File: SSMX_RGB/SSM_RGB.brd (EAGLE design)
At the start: 102.7 x 69.8 mm, 24 parts, among them IC1 CBT3244ADW, IC2 CBT3244ADW, IC3 CBT3244ADW, IC4 CBT3244ADW, U1 L7805C-V

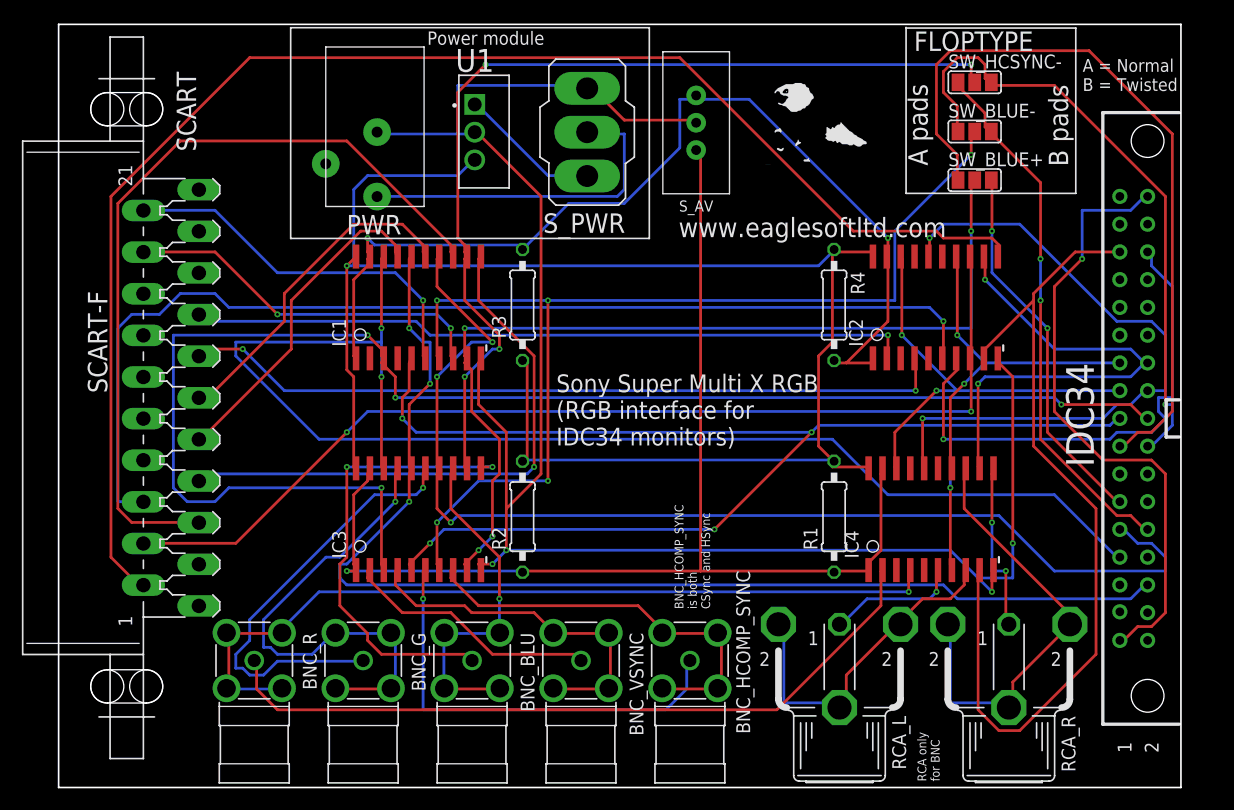
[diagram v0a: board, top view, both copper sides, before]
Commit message: Revision
*Tied S_PWR Pos 1 to nothing (no power on this pos)
*Addressed errors and warnings in ERC
*Ran Autorouter again to fix netlist
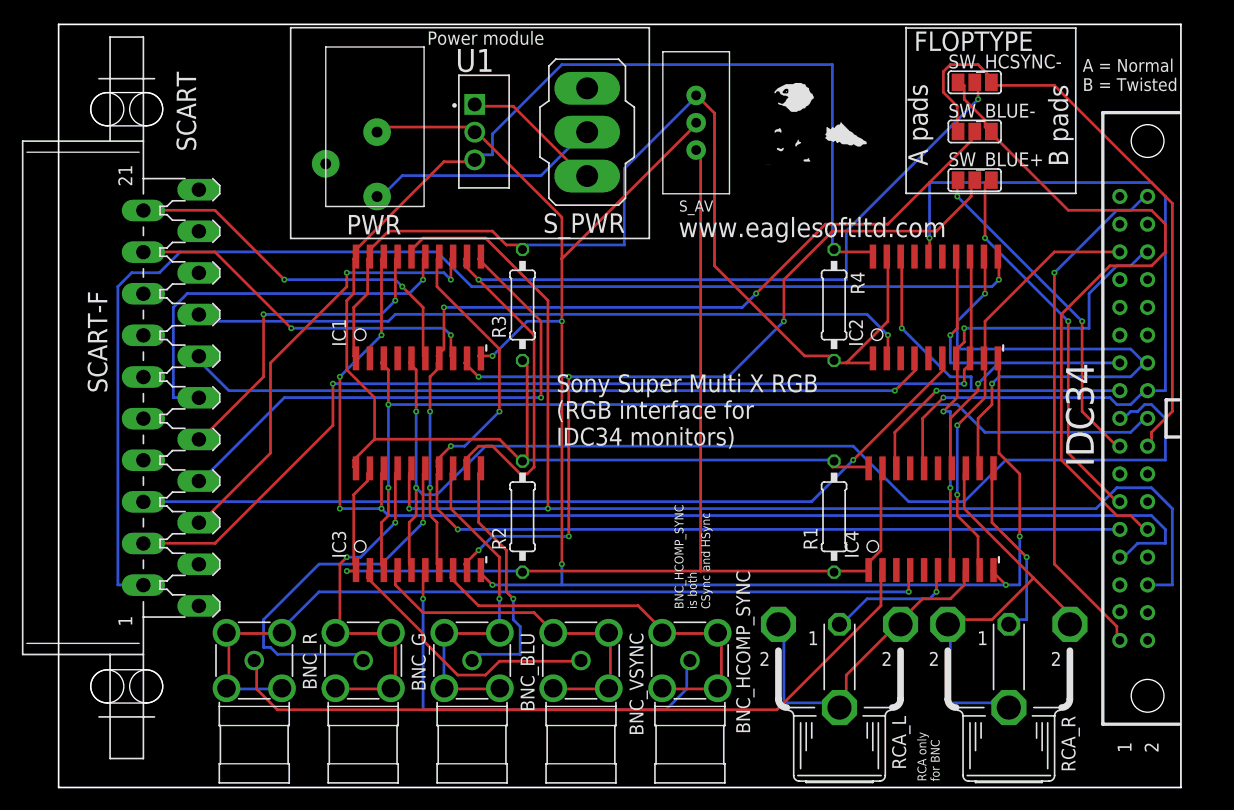
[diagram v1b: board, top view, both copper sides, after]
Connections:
- net BUS_V-: no longer S_PWR.1
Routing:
- net GREEN-: track 136.0 -> 91.1 mm, vias 4 -> 2
- net AUDIO_R+: track 79.4 -> 39.6 mm, vias 0 -> 2
- net P15: track 68.2 -> 30.7 mm, vias 0 -> 2
- net SC_BLUE-: track 73.8 -> 40.6 mm, vias 0 -> 2
- net SC_AUDIO_L+: track 99.6 -> 79.3 mm
- net BNC_BLU+: track 42.7 -> 23.3 mm, vias 2 -> 1
- net BLUE-: track 98.5 -> 80.6 mm, vias 5 -> 4
- net SC_AUDIO_R+: track 131.8 -> 115.3 mm, vias 0 -> 1
- net BUS_V-: track 169.5 -> 154.8 mm, vias 4 -> 6
- net P10: track 49.1 -> 63.8 mm, vias 2 -> 0
- net RED-: track 61.0 -> 75.1 mm
- net AUDIO_R-: track 59.0 -> 45.2 mm, vias 2 -> 3
- net HCSYNC+: track 104.7 -> 92.1 mm
- net VSYNC+: track 122.7 -> 110.8 mm, vias 2 -> 4
- net BNC_G-: track 45.6 -> 33.8 mm, vias 1 -> 2
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
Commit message: Final PCB revisions
SSM & X:
*Renamed BNC_HComp_Sync to just BNC_HCSYNC
*Renamed "Normal" cable type to "Nonstd"
*Removed stray line segs in PCB Art

SSM:
*Added warning about using both AV sources

X:
*Renamed VReg and Bus Sw IC components to Ux series
*Renamed both switchs to Sx series
*Renamed "PWR" to "J1"

Documentation:
*1st draft. Needs final product photos/images, and list of component names+parts
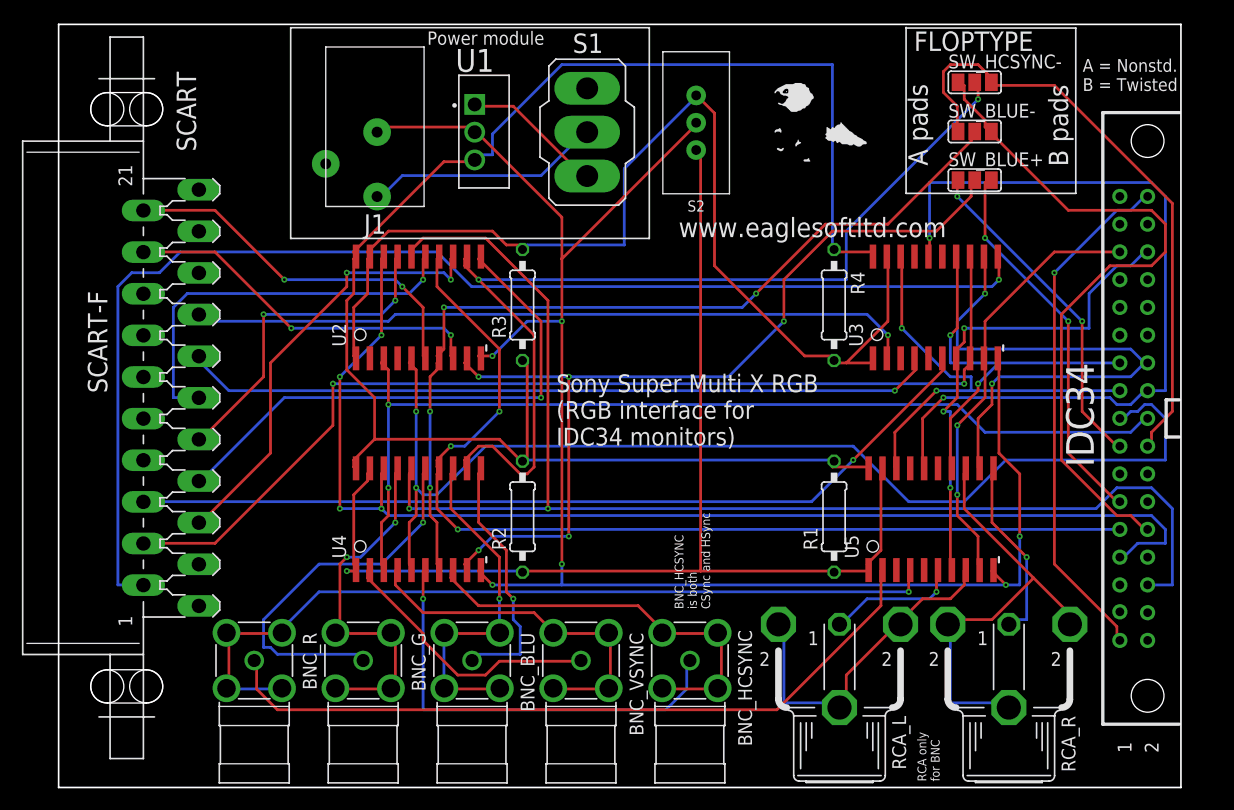
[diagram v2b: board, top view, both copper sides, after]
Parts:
- RCA_L: value J1 -> (none)
- RCA_R: value J2 -> (none)
- renumbered BNC_HCOMP_SYNC to BNC_HCSYNC, IC1 to U2, IC2 to U3, IC3 to U4, IC4 to U5, PWR to J1, S_AV to S2, S_PWR to S1
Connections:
- net BNC_HCOMP_SYNC+ renamed BNC_HCSYNC+
- net BNC_HCOMP_SYNC- renamed BNC_HCSYNC-
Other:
- board text added: "A = Nonstd. B = Twisted"
- board text added: "BNC_HCSYNC is both CSync and HSync"
- board text added: "J1"
- board text removed: "A = Normal B = Twisted"
- board text removed: "BNC_HCOMP_SYNC is both CSync and HSync"
- board text removed: "C:/Users/Anthony/Documents/eagle/SSM/Artwork/Large/p1m.bmp"
- board text removed: "C:/Users/Anthony/Documents/eagle/SSM/Artwork/Large/p2m.bmp"
- board text removed: "C:/Users/Anthony/Documents/eagle/SSM/Artwork/Large/p3m.bmp"
- board text removed: "PWR"

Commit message: Updated pics, manual, BOM
*Updated manuals with footprint names/labels for directions
*Updated project artwork
*Updated a trace on SSMX board, so that it doesn't go through copper-clad Eagle PCB
*Updated BOM with more accurate, nearly final pricing. Added bagging costs. floppy cable costs
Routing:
- net BUS_V+: track 152.0 -> 147.5 mm
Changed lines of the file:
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@@
 <wire x1="84.455" y1="83.82" x2="84.66455" y2="83.39105" width="0.254" layer="1"/>
 <wire x1="95.25" y1="92.075" x2="95.5294" y2="92.2401" width="0.254" layer="1"/>
-<wire x1="128.27" y1="100.965" x2="128.27" y2="84.455" width="0.254" layer="16"/>
-<wire x1="103.505" y1="100.965" x2="128.27" y2="100.965" width="0.254" layer="16"/>
+<wire x1="120.65" y1="100.965" x2="120.65" y2="95.12935" width="0.254" layer="16"/>
+<wire x1="120.65" y1="95.12935" x2="128.2319" y2="87.54745" width="0.254" layer="16"/>
+<wire x1="128.2319" y1="87.54745" x2="128.27" y2="84.455" width="0.254" layer="16"/>
+<wire x1="103.505" y1="100.965" x2="120.65" y2="100.965" width="0.254" layer="16"/>
 <wire x1="97.155" y1="94.615" x2="103.505" y2="100.965" width="0.254" layer="16"/>
 <wire x1="97.155" y1="92.71" x2="97.155" y2="94.615" width="0.254" layer="16"/>
